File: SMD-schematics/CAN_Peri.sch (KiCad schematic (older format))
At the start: 6 parts, among them J5 Screw_Terminal_01x02, U3 MCP2551-I/P

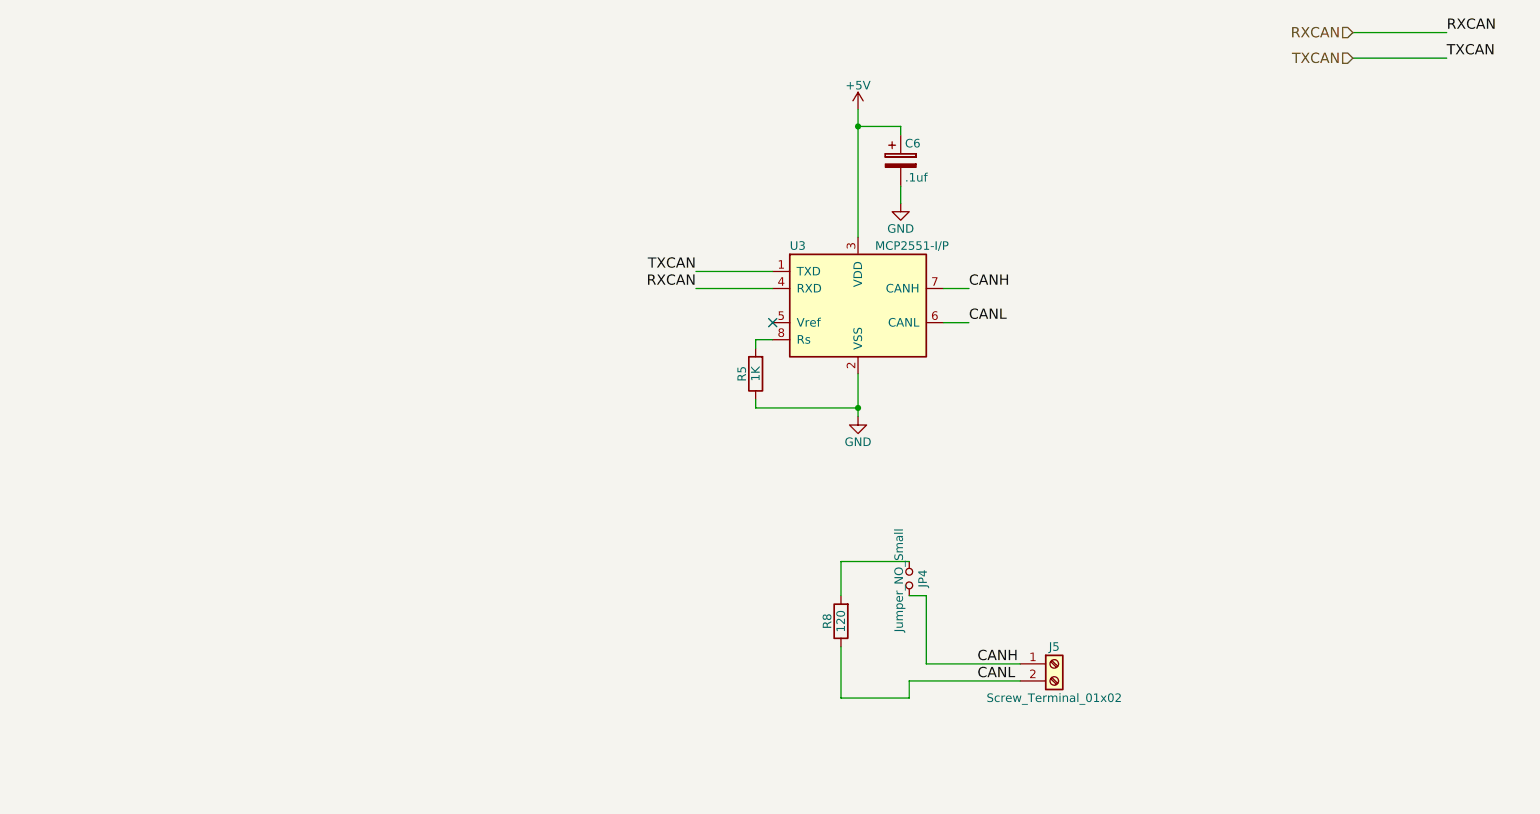
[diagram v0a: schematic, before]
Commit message: adding lin circuit to the schematic
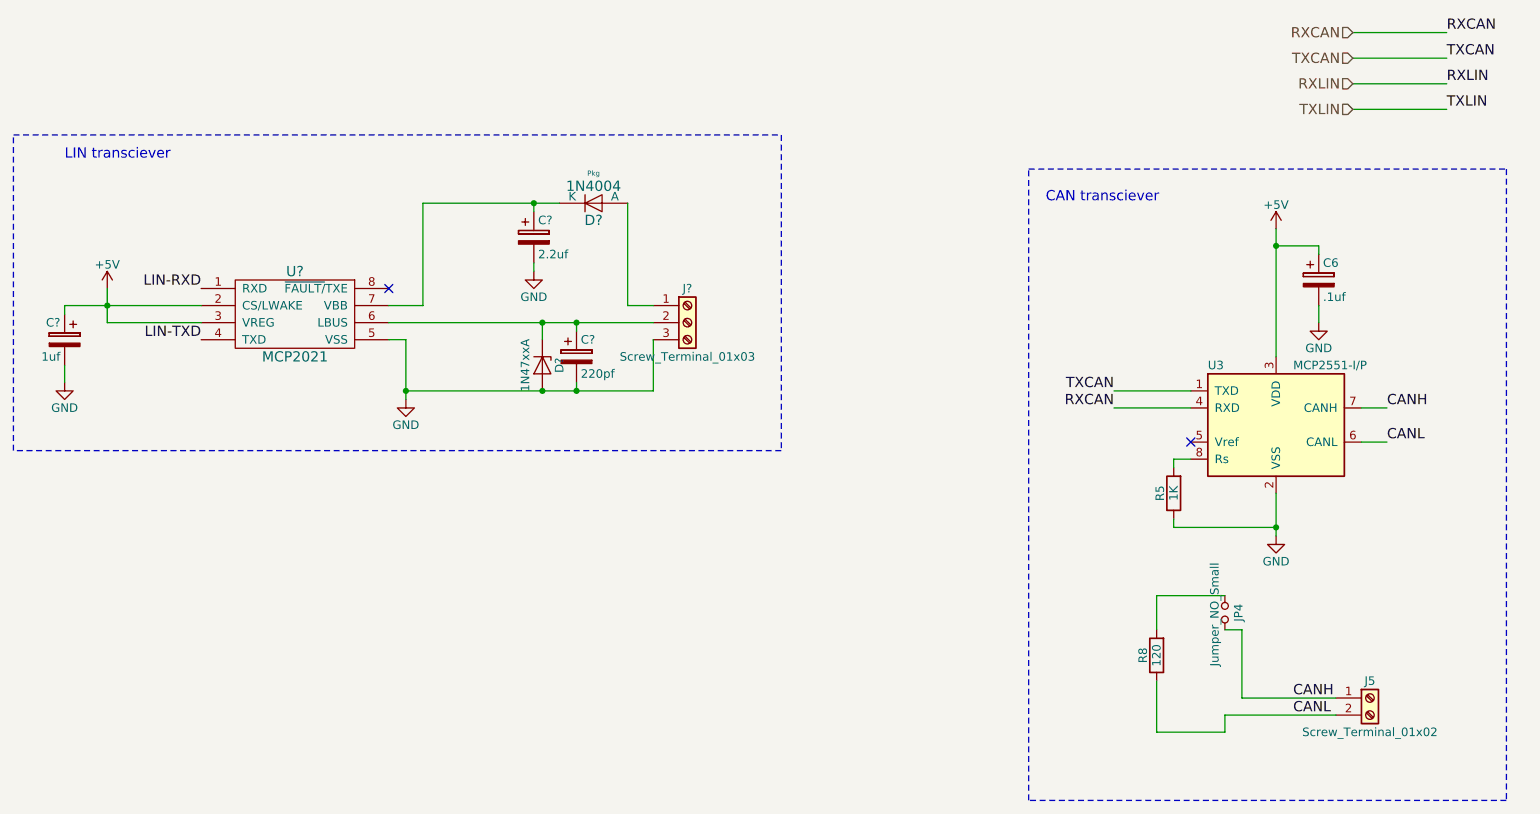
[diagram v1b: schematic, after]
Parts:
- added C?: 1uf, Capacitors_SMD:CP_Elec_8x6.5, symbol CP
- added C?: 2.2uf, Capacitors_SMD:CP_Elec_8x6.5, symbol CP
- added C?: 220pf, Capacitors_SMD:CP_Elec_8x6.5, symbol CP
- added D?: 1N4004, Pkg, symbol 1N4004
- added D?: 1N47xxA, Diode_THT:D_DO-41_SOD81_P10.16mm_Horizontal, symbol 1N47xxA
- added J?: Screw_Terminal_01x03, symbol Screw_Terminal_01x03
- added U?: MCP2021, symbol MCP2021
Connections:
- net +5V: now also C?.1, U?.2 (CS/LWAKE), U?.3 (VREG)
- net GND: now also C?.2, C?.2, C?.2, D?.2 (A), J?.3 (Pin_3), U?.5 (VSS)
- new net: C?.1, D?.1 (K), J?.2 (Pin_2), U?.6 (LBUS)
- new net: C?.1, D?.K, U?.7 (VBB)
- new net: D?.A, J?.1 (Pin_1)
- new net LIN-RXD: U?.1 (RXD)
- new net LIN-TXD: U?.4 (TXD)
- no-connect marks 1 -> 2
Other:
- note added: "CAN transciever"
- note added: "LIN transciever"
- moved on the sheet: C6, J5, JP4, R5, R8, U3

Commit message: adding lin circuit to the scgematic without the diode
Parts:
- removed D?: 1N4004, Pkg, symbol 1N4004
- D4: renamed from D?; footprint Diode_THT:D_DO-41_SOD81_P10.16mm_Horizontal -> Diodes_SMD:D_SOT-23_ANK
- J11: renamed from J?; footprint (none) -> TerminalBlocks_Phoenix:TerminalBlock_Phoenix_MKDS1.5-3pol
- U4: renamed from U?; footprint (none) -> Housings_SOIC:SOIC-8_3.9x4.9mm_Pitch1.27mm
- gave numbers to parts that had none: 3
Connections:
- net LIN-RXD is gone; now on net RXLIN: U4.1 (RXD)
- net LIN-TXD is gone; now on net TXLIN: U4.4 (TXD)
- net at C4.1, U4.7 (VBB): now also J11.1 (Pin_1)
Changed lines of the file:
@@
 CAN transciever
 $Comp
-L MCP2021 U?
+L MCP2021 U4
 U 1 1 5AD516AF
 P 3150 2550
-F 0 "U?" H 3150 2800 60  0000 C CNN
+F 0 "U4" H 3150 2800 60  0000 C CNN
 F 1 "MCP2021" H 3150 2300 60  0000 C CNN
-F 2 "" H 3000 2550 60  0001 C CNN
+F 2 "Housings_SOIC:SOIC-8_3.9x4.9mm_Pitch1.27mm" H 3000 2550 60  0001 C CNN
 F 3 "" H 3000 2550 60  0001 C CNN
 	1    3150 2550
@@
 NoConn ~ 3700 2400
 $Comp
-L GND #PWR?
+L GND #PWR033
 U 1 1 5AD51872
 P 3800 3050
-F 0 "#PWR?" H 3800 2800 50  0001 C CNN
+F 0 "#PWR033" H 3800 2800 50  0001 C CNN
 F 1 "GND" H 3800 2900 50  0000 C CNN
 F 2 "" H 3800 3050 50  0001 C CNN
@@
 	3800 2700 3700 2700
 $Comp
-L +5V #PWR?
+L +5V #PWR034
 U 1 1 5AD51A7F
 P 2050 2400
-F 0 "#PWR?" H 2050 2250 50  0001 C CNN
+F 0 "#PWR034" H 2050 2250 50  0001 C CNN
 F 1 "+5V" H 2050 2540 50  0000 C CNN
 F 2 "" H 2050 2400 50  0001 C CNN
@@
 $EndComp
 $Comp
-L GND #PWR?
+L GND #PWR035
 U 1 1 5AD51A85
 P 1800 2950
-F 0 "#PWR?" H 1800 2700 50  0001 C CNN
+F 0 "#PWR035" H 1800 2700 50  0001 C CNN
 F 1 "GND" H 1800 2800 50  0000 C CNN
 F 2 "" H 1800 2950 50  0001 C CNN
@@
 $EndComp
 $Comp
-L CP C?
+L CP C3
 U 1 1 5AD51A8B
 P 1800 2700
-F 0 "C?" H 1825 2800 50  0000 L CNN
+F 0 "C3" H 1825 2800 50  0000 L CNN
 F 1 "1uf" H 1825 2600 50  0000 L CNN
 F 2 "Capacitors_SMD:CP_Elec_8x6.5" H 1838 2550 50  0001 C CNN
@@
 Wire Wire Line
 	2050 2400 2050 2600
-Wire Wire Line
-	1800 2500 2600 2500
 Connection ~ 2050 2500
 Wire Wire Line
@@
 	1800 2850 1800 2950
 $Comp
-L 1N4004 D?
-U 1 1 5AD51DD1
-P 4900 1900
-F 0 "D?" H 4900 2000 60  0000 C CNN
-F 1 "1N4004" H 4900 1800 60  0000 C CNN
-F 2 "Pkg" H 4900 1725 30  0000 C CNN
-F 3 "" H 4900 1900 50  0000 C CNN
-	1    4900 1900
-	-1   0    0    1
-$EndComp
-$Comp
-L Screw_Terminal_01x03 J?
+L Screw_Terminal_01x03 J11
 U 1 1 5AD520C8
 P 5450 2600
-F 0 "J?" H 5450 2800 50  0000 C CNN
+F 0 "J11" H 5450 2800 50  0000 C CNN
 F 1 "Screw_Terminal_01x03" H 5450 2400 50  0000 C CNN
-F 2 "" H 5450 2600 50  0001 C CNN
+F 2 "TerminalBlocks_Phoenix:TerminalBlock_Phoenix_MKDS1.5-3pol" H 5450 2600 50  0001 C CNN
 F 3 "" H 5450 2600 50  0001 C CNN
 	1    5450 2600
@@
 	3700 2600 5250 2600
 Wire Wire Line
-	5100 1900 5100 2500
-Wire Wire Line
 	5100 2500 5250 2500
 $Comp
-L CP C?
+L CP C4
 U 1 1 5AD52F3D
 P 4550 2100
-F 0 "C?" H 4575 2200 50  0000 L CNN
+F 0 "C4" H 4575 2200 50  0000 L CNN
 F 1 "2.2uf" H 4575 2000 50  0000 L CNN
 F 2 "Capacitors_SMD:CP_Elec_8x6.5" H 4588 1950 50  0001 C CNN
@@
 	4550 1950 4550 1900
 Wire Wire Line
-	3900 1900 4700 1900
+	3900 1900 5100 1900
 $Comp
-L GND #PWR?
+L GND #PWR036
 U 1 1 5AD530BE
 P 4550 2300
-F 0 "#PWR?" H 4550 2050 50  0001 C CNN
+F 0 "#PWR036" H 4550 2050 50  0001 C CNN
 F 1 "GND" H 4550 2150 50  0000 C CNN
 F 2 "" H 4550 2300 50  0001 C CNN
@@
 Wire Wire Line
 	4550 2300 4550 2250
-Wire Wire Line
-	3900 1900 3900 2500
-Wire Wire Line
-	3900 2500 3700 2500
 Connection ~ 4550 1900
 $Comp
-L 1N47xxA D?
+L 1N47xxA D4
 U 1 1 5AD53174
 P 4600 2850
-F 0 "D?" H 4600 2950 50  0000 C CNN
+F 0 "D4" H 4600 2950 50  0000 C CNN
 F 1 "1N47xxA" H 4600 2750 50  0000 C CNN
-F 2 "Diode_THT:D_DO-41_SOD81_P10.16mm_Horizontal" H 4600 2675 50  0001 C CNN
+F 2 "Diodes_SMD:D_SOT-23_ANK" H 4600 2675 50  0001 C CNN
 F 3 "" H 4600 2850 50  0001 C CNN
 	1    4600 2850
@@
 Connection ~ 4600 3000
 $Comp
-L CP C?
+L CP C5
 U 1 1 5AD532A4
 P 4800 2800
-F 0 "C?" H 4825 2900 50  0000 L CNN
+F 0 "C5" H 4825 2900 50  0000 L CNN
 F 1 "220pf" H 4825 2700 50  0000 L CNN
 F 2 "Capacitors_SMD:CP_Elec_8x6.5" H 4838 2650 50  0001 C CNN
@@
 Wire Wire Line
 	2050 2600 2600 2600
-Wire Wire Line
-	2100 2500 2100 2500
-Text Label 2600 2400 2    60   ~ 0
+Text Label 2500 2400 2    60   ~ 0
 LIN-RXD
-Text Label 2600 2700 2    60   ~ 0
+Text Label 2500 2700 2    60   ~ 0
 LIN-TXD
 Wire Notes Line
@@
 TXLIN
 Text Label 9900 1200 0    60   ~ 0
-RXLIN
+LIN-RXD
 Text Label 9900 1350 0    60   ~ 0
-TXLIN
+LIN-TXD
 Wire Wire Line
 	9900 1350 9350 1350
 Wire Wire Line
 	9350 1200 9900 1200
+Wire Wire Line
+	1800 2500 2600 2500
+Wire Wire Line
+	2500 2700 2600 2700
+Wire Wire Line
+	2600 2400 2500 2400
+Wire Wire Line
+	3900 1900 3900 2500
+Wire Wire Line
+	3900 2500 3700 2500
+Wire Wire Line
+	5100 1900 5100 2500
 $EndSCHEMATC
